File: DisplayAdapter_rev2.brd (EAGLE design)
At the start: 21.8 x 24.2 mm, 2 parts

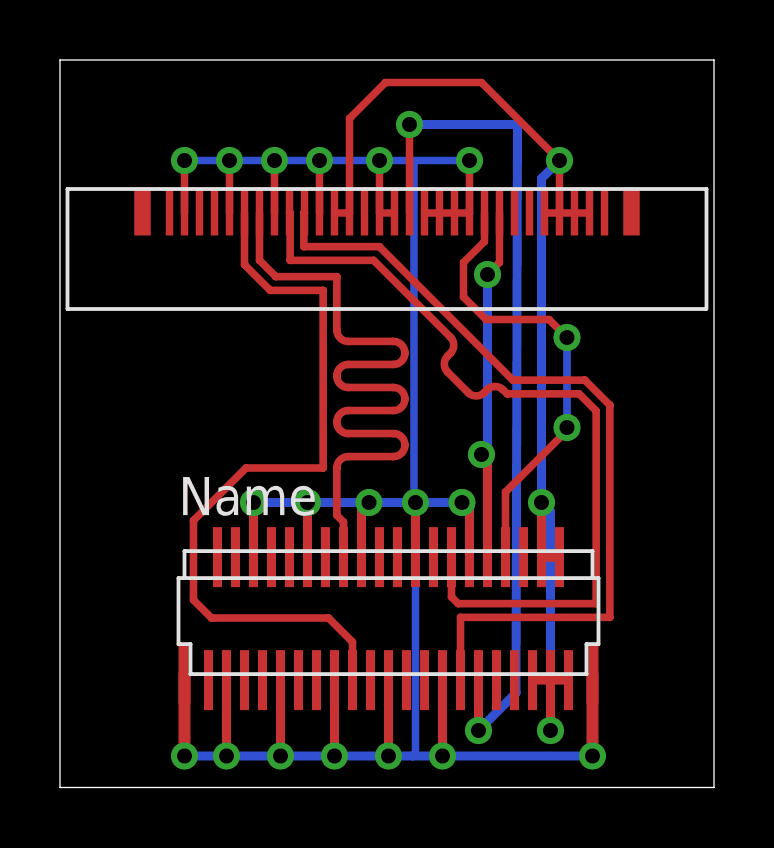
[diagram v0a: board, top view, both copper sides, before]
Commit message: redone pcb routing
pcb routing for the display adapter should now be correct
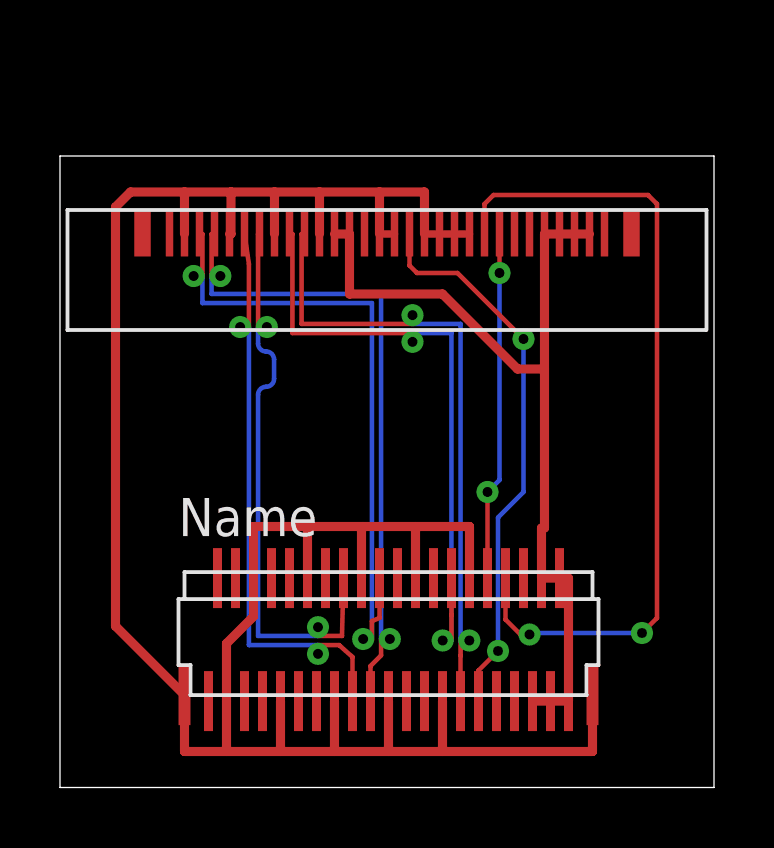
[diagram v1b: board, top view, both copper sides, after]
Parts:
- moved U$1 0.70 mm to (10.9, 4.48)
- moved U$2 0.70 mm to (10.9, 17.2)
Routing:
- net LANE1_N: track 0.00 -> 22.7 mm, vias 0 -> 2
- net LANE1_P: track 0.00 -> 22.6 mm, vias 0 -> 2
- net N$11: track 15.3 -> 27.7 mm
- net N$7: track 28.9 -> 18.6 mm
- net N$9: track 40.1 -> 30.3 mm, vias 3 -> 0
- net N$10: track 89.9 -> 84.3 mm, vias 18 -> 0
- net AUX_CH_N: track 27.7 -> 22.1 mm, vias 0 -> 2
- net LANE0_N: track 25.5 -> 20.0 mm, vias 0 -> 2
- net AUX_CH_P: track 27.4 -> 22.2 mm, vias 0 -> 2
- net LANE0_P: track 24.8 -> 19.8 mm, vias 0 -> 2
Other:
- board size 21.8 x 24.2 mm -> 21.8 x 21.1 mm
